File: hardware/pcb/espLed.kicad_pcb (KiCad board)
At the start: 2 copper layers, 23 parts, among them J1 led_strip, J2 flashing, J3 power, Q1 IRF9310TRPBF, Q2 AO3400A, Q3 AO3400A, Q4 AO3400A, SW1 reset, SW2 flash, U1 AMS1117-3.3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

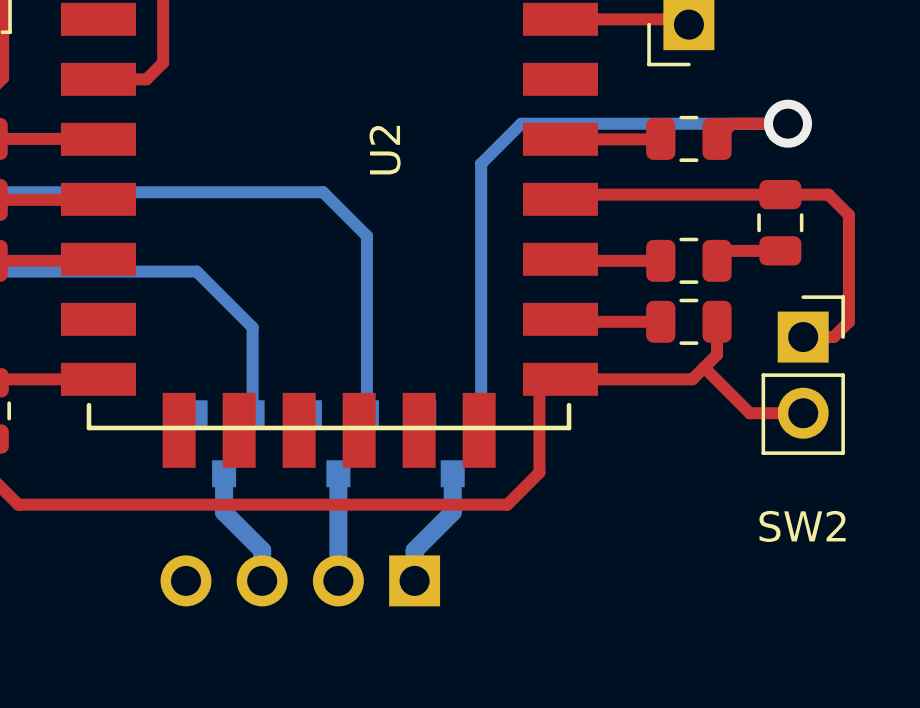
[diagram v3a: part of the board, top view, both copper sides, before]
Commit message: move the 'flash' jumper to save a bit of space
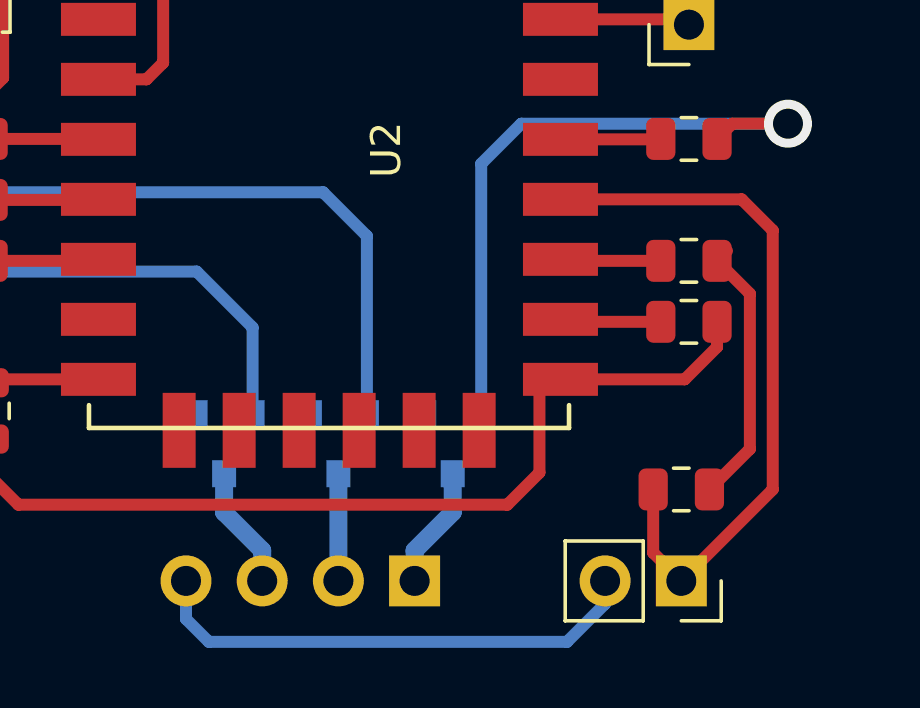
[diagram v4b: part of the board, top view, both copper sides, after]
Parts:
- moved R7 9.48 mm to (191.0, 135.9), turned to 180 degrees
- moved SW2 9.09 mm to (191.0, 138.9), turned to 270 degrees
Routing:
- net GND: track 62.3 -> 75.1 mm
- net Net-(R7-Pad2): track 16.0 -> 24.8 mm
- net +3V3: track 17.4 -> 24.3 mm
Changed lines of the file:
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@@
     (thickness 1.6)
     (drawings 0)
-    (tracks 115)
+    (tracks 119)
     (zones 0)
     (modules 23)
@@
     (pad_to_mask_clearance 0.05)
     (aux_axis_origin 0 0)
-    (visible_elements FFFFFF7F)
+    (visible_elements FFFFF77F)
     (pcbplotparams
       (layerselection 0x010fc_ffffffff)
@@
   )
   (module Connector_PinSocket_2.54mm:PinSocket_1x02_P2.54mm_Vertical (layer F.Cu)
-    (at 195.072 130.81)
+    (at 191.008 138.938 270)
     (descr "Through hole straight socket strip, 1x02, 2.54mm pitch, single row (from Kicad 4.0.7), script generated")
     (tags "Through hole socket strip THT 1x02 2.54mm single row")
-    (fp_text reference SW2 (at 0 6.35) (layer F.SilkS)
-      (effects (font (size 1 1) (thickness 0.15)))
-    )
-    (fp_text value flash (at 0 5.08) (layer F.Fab)
+    (fp_text reference SW2 (at 4.318 1.27 180) (layer F.SilkS) hide
+      (effects (font (size 1 1) (thickness 0.15)))
+    )
+    (fp_text value flash (at 0 -2.54 270) (layer F.Fab)
       (effects (font (size 1 1) (thickness 0.15)))
     )
@@
     (fp_line (start 0.635 -1.27) (end 1.27 -0.635) (layer F.Fab) (width 0.1))
     (fp_line (start -1.27 -1.27) (end 0.635 -1.27) (layer F.Fab) (width 0.1))
-    (fp_text user %R (at 0 1.27) (layer F.Fab) hide
-      (effects (font (size 1 1) (thickness 0.15)))
-    )
-    (pad 2 thru_hole oval (at 0 2.54) (size 1.7 1.7) (drill 1) (layers *.Cu *.Mask)
-      (net 1 GND))
-    (pad 1 thru_hole rect (at 0 0) (size 1.7 1.7) (drill 1) (layers *.Cu *.Mask)
+    (fp_text user %R (at 0 1.27 90) (layer F.Fab) hide
+      (effects (font (size 1 1) (thickness 0.15)))
+    )
+    (pad 2 thru_hole oval (at 0 2.54 270) (size 1.7 1.7) (drill 1) (layers *.Cu *.Mask)
+      (net 1 GND))
+    (pad 1 thru_hole rect (at 0 0 270) (size 1.7 1.7) (drill 1) (layers *.Cu *.Mask)
       (net 19 "Net-(R7-Pad2)"))
     (model ${KISYS3DMOD}/Connector_PinSocket_2.54mm.3dshapes/PinSocket_1x02_P2.54mm_Vertical.wrl
@@
   )
   (module Resistor_SMD:R_0805_2012Metric (layer F.Cu)
-    (at 194.31 127 90)
+    (at 191.008 135.89 180)
     (descr "Resistor SMD 0805 (2012 Metric), square (rectangular) end terminal, IPC_7351 nominal, (Body size source: https://docs.google.com/spreadsheets/d/1BsfQQcO9C6DZCsRaXUlFlo91Tg2WpOkGARC1WS5S8t0/edit?usp=sharing), generated with kicad-footprint-generator")
     (tags resistor)
     (attr smd)
-    (fp_text reference R7 (at 0 -1.65 90) (layer F.SilkS) hide
-      (effects (font (size 1 1) (thickness 0.15)))
-    )
-    (fp_text value 10k (at 0 1.65 90) (layer F.Fab) hide
+    (fp_text reference R7 (at 0 -1.65) (layer F.SilkS) hide
+      (effects (font (size 1 1) (thickness 0.15)))
+    )
+    (fp_text value 10k (at 0 1.65) (layer F.Fab) hide
       (effects (font (size 1 1) (thickness 0.15)))
     )
@@
     (fp_line (start -1 -0.6) (end 1 -0.6) (layer F.Fab) (width 0.1))
     (fp_line (start -1 0.6) (end -1 -0.6) (layer F.Fab) (width 0.1))
-    (fp_text user %R (at 0 0 90) (layer F.Fab) hide
+    (fp_text user %R (at 0 0) (layer F.Fab) hide
       (effects (font (size 0.5 0.5) (thickness 0.08)))
     )
-    (pad 2 smd roundrect (at 0.9375 0 90) (size 0.975 1.4) (layers F.Cu F.Paste F.Mask) (roundrect_rratio 0.25)
+    (pad 2 smd roundrect (at 0.9375 0 180) (size 0.975 1.4) (layers F.Cu F.Paste F.Mask) (roundrect_rratio 0.25)
       (net 19 "Net-(R7-Pad2)"))
-    (pad 1 smd roundrect (at -0.9375 0 90) (size 0.975 1.4) (layers F.Cu F.Paste F.Mask) (roundrect_rratio 0.25)
+    (pad 1 smd roundrect (at -0.9375 0 180) (size 0.975 1.4) (layers F.Cu F.Paste F.Mask) (roundrect_rratio 0.25)
       (net 3 +3V3))
     (model ${KISYS3DMOD}/Resistor_SMD.3dshapes/R_0805_2012Metric.wrl
@@
   (segment (start 167.894 135.382) (end 168.91 136.398) (width 0.4) (layer F.Cu) (net 1))
   (segment (start 167.894 134.209) (end 167.894 135.382) (width 0.4) (layer F.Cu) (net 1))
-  (segment (start 191.376 132.22) (end 186.28 132.22) (width 0.4) (layer F.Cu) (net 1))
-  (segment (start 192.1995 130.302) (end 192.1995 131.3965) (width 0.4) (layer F.Cu) (net 1))
-  (segment (start 193.294 133.35) (end 191.77 131.826) (width 0.4) (layer F.Cu) (net 1))
-  (segment (start 195.072 133.35) (end 193.294 133.35) (width 0.4) (layer F.Cu) (net 1))
-  (segment (start 191.77 131.826) (end 191.376 132.22) (width 0.4) (layer F.Cu) (net 1))
-  (segment (start 192.1995 131.3965) (end 191.77 131.826) (width 0.4) (layer F.Cu) (net 1))
+  (segment (start 192.1995 131.1425) (end 192.1995 130.302) (width 0.4) (layer F.Cu) (net 1))
+  (segment (start 191.122 132.22) (end 192.1995 131.1425) (width 0.4) (layer F.Cu) (net 1))
+  (segment (start 186.28 132.22) (end 191.122 132.22) (width 0.4) (layer F.Cu) (net 1))
+  (segment (start 174.498 140.208) (end 174.498 138.938) (width 0.4) (layer B.Cu) (net 1))
+  (segment (start 175.26 140.97) (end 174.498 140.208) (width 0.4) (layer B.Cu) (net 1))
+  (segment (start 187.198 140.97) (end 175.26 140.97) (width 0.4) (layer B.Cu) (net 1))
+  (segment (start 188.468 139.7) (end 187.198 140.97) (width 0.4) (layer B.Cu) (net 1))
+  (segment (start 188.468 138.938) (end 188.468 139.7) (width 0.4) (layer B.Cu) (net 1))
   (segment (start 47.75 71.95) (end 47.8 71.9) (width 0.4) (layer F.Cu) (net 2))
   (segment (start 47.75 74.3125) (end 47.75 71.95) (width 0.4) (layer F.Cu) (net 2))
@@
   (segment (start 172.28 132.22) (end 168.008 132.22) (width 0.4) (layer F.Cu) (net 3))
   (segment (start 192.532 127.9375) (end 192.1995 128.27) (width 0.4) (layer F.Cu) (net 3))
-  (segment (start 194.31 127.9375) (end 192.532 127.9375) (width 0.4) (layer F.Cu) (net 3))
   (segment (start 166.1945 110.49) (end 166.1945 112.522) (width 0.4) (layer F.Cu) (net 3))
+  (segment (start 193.294 134.5415) (end 191.9455 135.89) (width 0.4) (layer F.Cu) (net 3))
+  (segment (start 193.294 129.3645) (end 193.294 134.5415) (width 0.4) (layer F.Cu) (net 3))
+  (segment (start 192.1995 128.27) (end 193.294 129.3645) (width 0.4) (layer F.Cu) (net 3))
   (segment (start 175.768 136.652) (end 177.038 137.922) (width 0.6) (layer B.Cu) (net 4))
   (segment (start 177.038 137.922) (end 177.038 138.938) (width 0.6) (layer B.Cu) (net 4))
@@
   (segment (start 172.28 122.22) (end 173.182 122.22) (width 0.4) (layer F.Cu) (net 18))
   (segment (start 186.28 126.22) (end 186.298 126.238) (width 0.4) (layer F.Cu) (net 19))
-  (segment (start 196.088 130.81) (end 195.072 130.81) (width 0.4) (layer F.Cu) (net 19))
-  (segment (start 196.596 130.302) (end 196.088 130.81) (width 0.4) (layer F.Cu) (net 19))
-  (segment (start 195.9125 126.0625) (end 196.596 126.746) (width 0.4) (layer F.Cu) (net 19))
-  (segment (start 196.596 126.746) (end 196.596 130.302) (width 0.4) (layer F.Cu) (net 19))
-  (segment (start 194.31 126.0625) (end 195.9125 126.0625) (width 0.4) (layer F.Cu) (net 19))
   (segment (start 186.4375 126.0625) (end 186.28 126.22) (width 0.4) (layer F.Cu) (net 19))
-  (segment (start 194.31 126.0625) (end 186.4375 126.0625) (width 0.4) (layer F.Cu) (net 19))
+  (segment (start 190.0705 138.0005) (end 191.008 138.938) (width 0.4) (layer F.Cu) (net 19))
+  (segment (start 190.0705 135.89) (end 190.0705 138.0005) (width 0.4) (layer F.Cu) (net 19))
+  (segment (start 194.056 127.254) (end 194.056 135.89) (width 0.4) (layer F.Cu) (net 19))
+  (segment (start 193.022 126.22) (end 194.056 127.254) (width 0.4) (layer F.Cu) (net 19))
+  (segment (start 194.056 135.89) (end 191.008 138.938) (width 0.4) (layer F.Cu) (net 19))
+  (segment (start 186.28 126.22) (end 193.022 126.22) (width 0.4) (layer F.Cu) (net 19))
   (segment (start 186.33 128.27) (end 186.28 128.22) (width 0.4) (layer F.Cu) (net 20))
   (segment (start 190.3245 128.27) (end 186.33 128.27) (width 0.4) (layer F.Cu) (net 20))

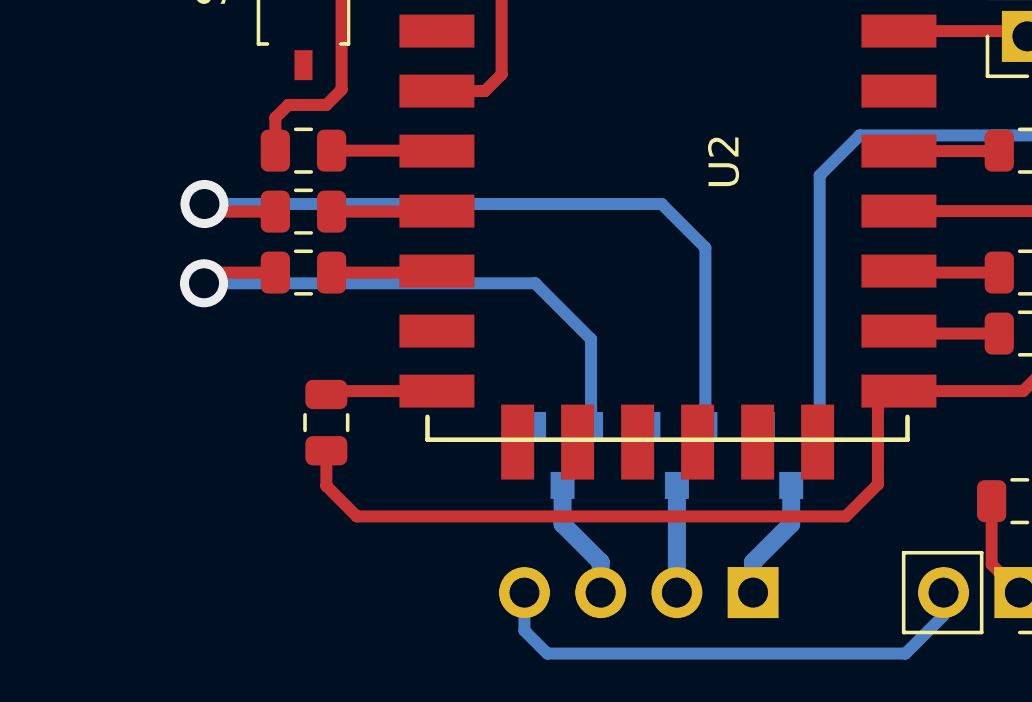
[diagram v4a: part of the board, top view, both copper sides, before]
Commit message: rearrange vias on the left side to save a bit of space
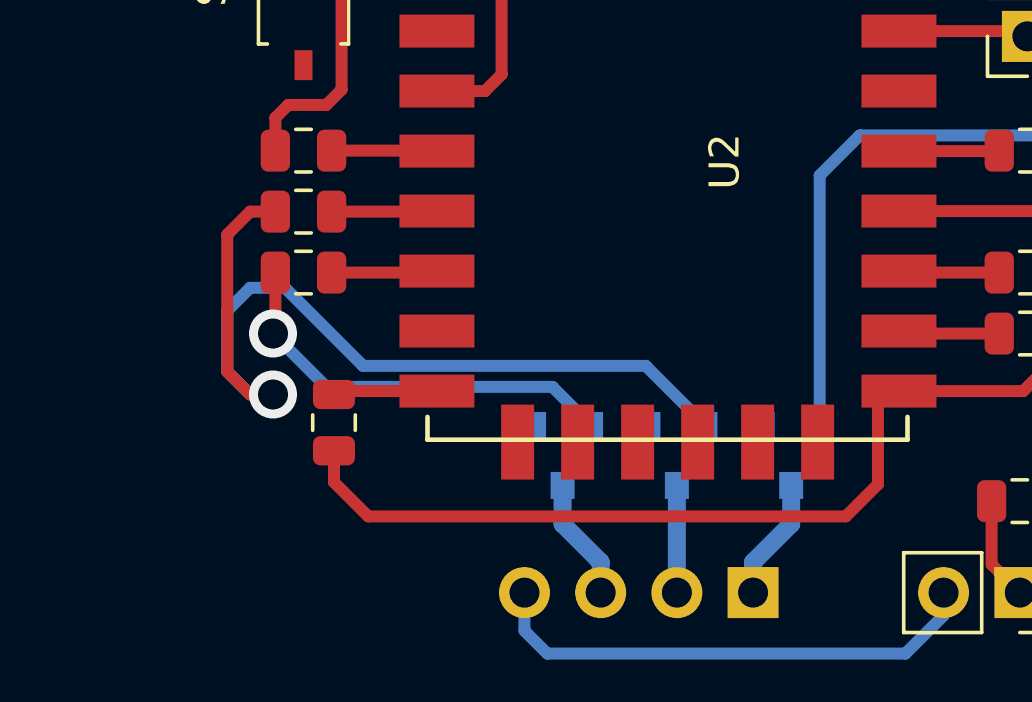
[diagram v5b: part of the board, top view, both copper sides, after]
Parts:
- moved C3 0.25 mm to (168.1, 133.3)
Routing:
- net Net-(Q4-Pad2): track 19.1 -> 13.9 mm
- net Net-(Q3-Pad2): track 25.7 -> 30.4 mm

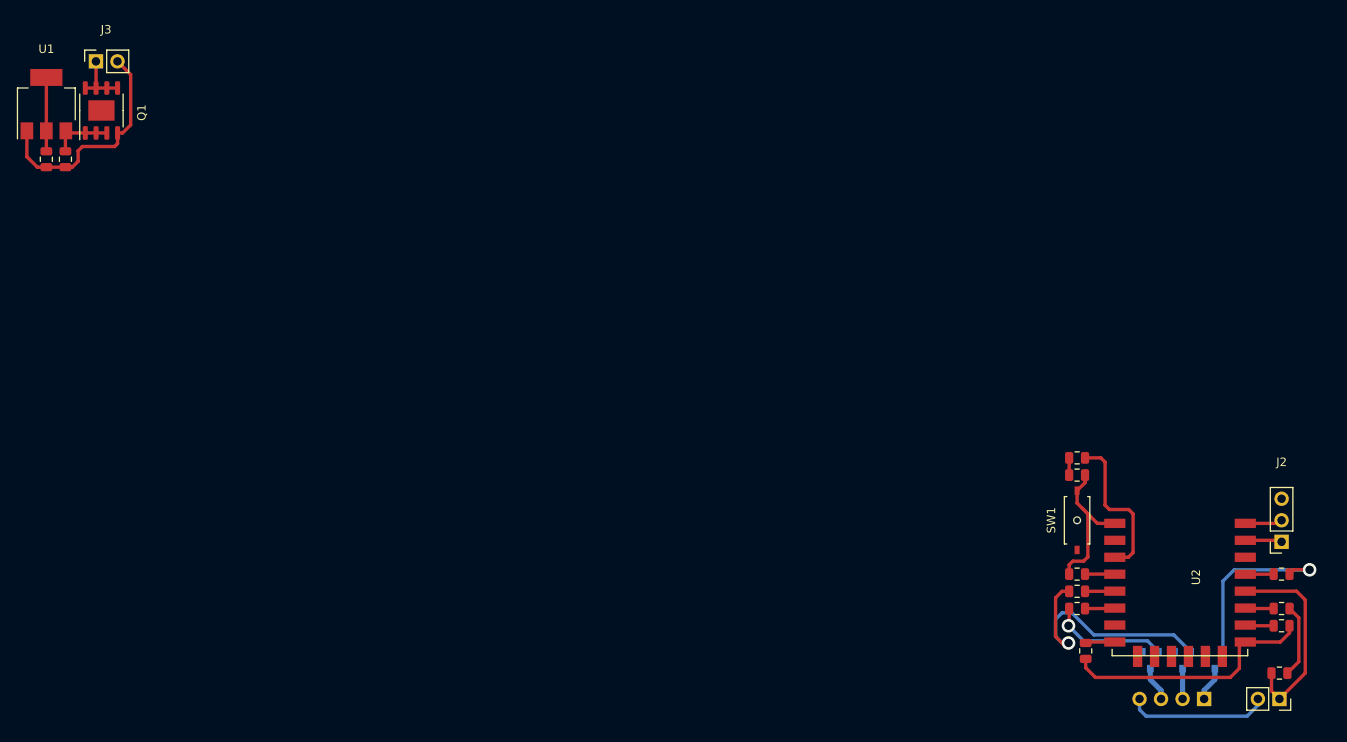
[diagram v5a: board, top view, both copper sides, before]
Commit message: arrange components on the right side tighter
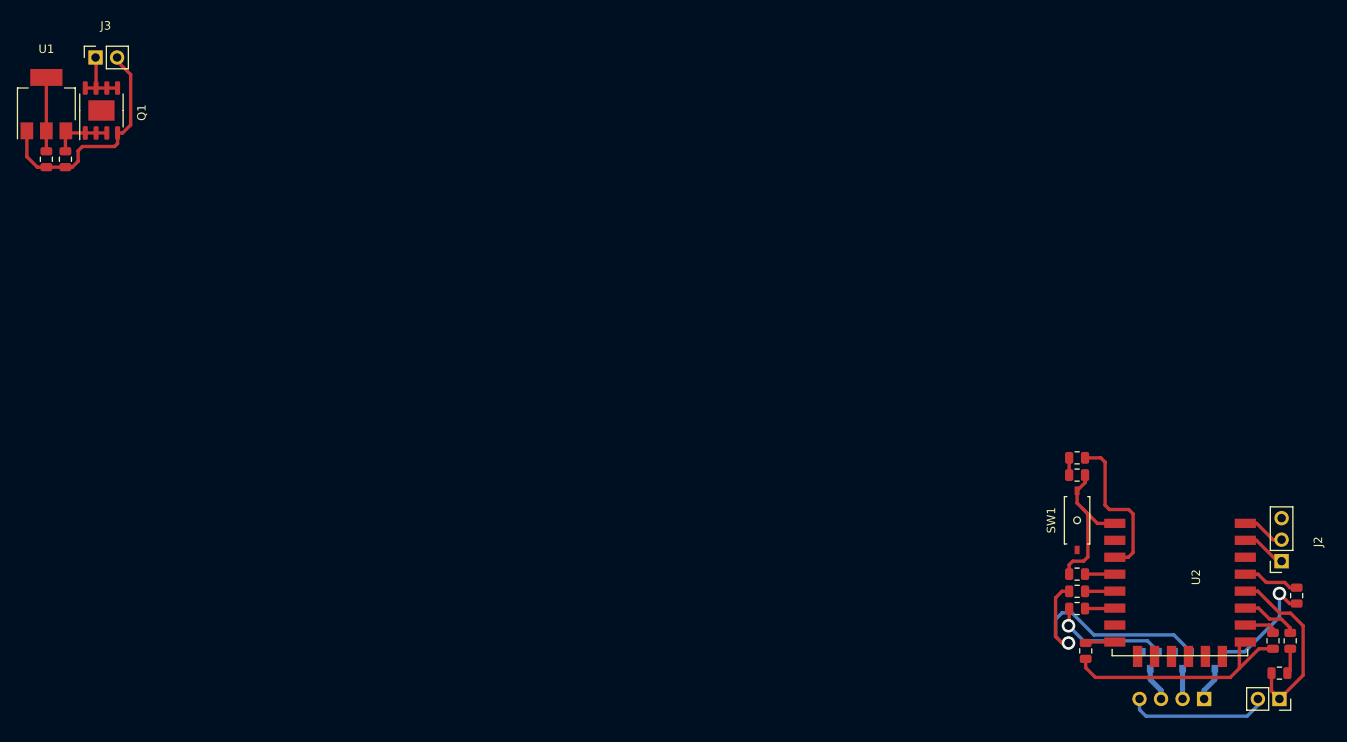
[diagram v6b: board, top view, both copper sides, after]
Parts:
- moved R8 3.94 mm to (192.3, 132.1), turned to 90 degrees
- moved R3 3.10 mm to (193.0, 126.7), turned to 90 degrees
- moved J2 2.29 mm to (191.3, 122.7)
- moved R9 2.05 mm to (190.2, 132.1), turned to 90 degrees
- moved J3 0.46 mm to (51.3, 63.2)
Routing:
- net Net-(Q2-Pad2): track 21.7 -> 13.7 mm
- net +3V3: track 24.3 -> 18.2 mm
- net Net-(R8-Pad2): track 4.07 -> 7.62 mm
- net /led1: track 4.07 -> 7.55 mm
- net GND: track 74.7 -> 72.5 mm
- net Net-(R7-Pad2): track 24.8 -> 22.7 mm
- net /TX: track 5.05 -> 6.00 mm
- net Net-(R9-Pad2): track 4.08 -> 4.75 mm
- net /RX: track 5.13 -> 5.78 mm

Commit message: place power part into it's position and connect some of the power pins
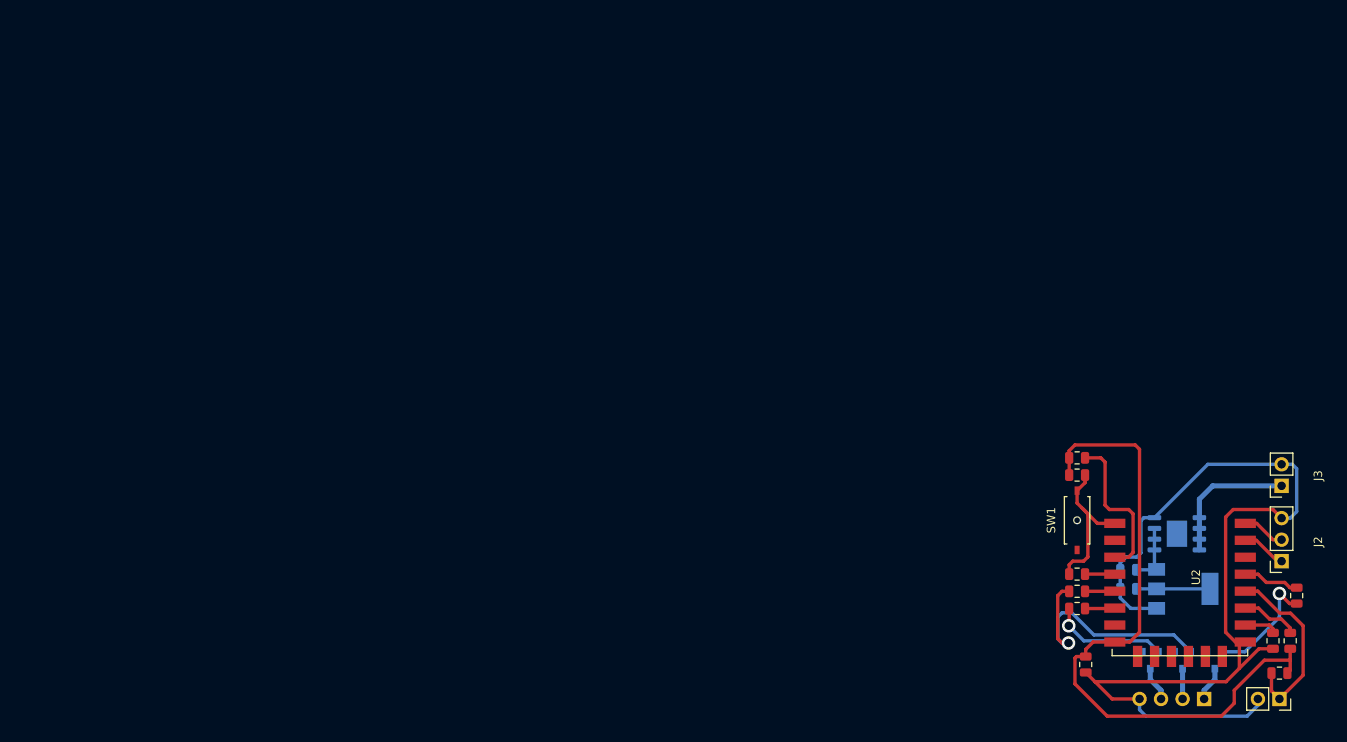
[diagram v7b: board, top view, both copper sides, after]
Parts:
- C1, C2, Q1, U1: moved to B.Cu
- moved J3 148.8 mm to (191.3, 113.8), turned to 180 degrees
- moved U1 145.8 mm to (179.7, 126.0), turned to 0 degrees
- moved C2 137.4 mm to (173.2, 126.0), turned to 180 degrees
- moved Q1 136.4 mm to (178.9, 119.5), turned to 0 degrees
- moved C1 134.4 mm to (173.2, 123.7), turned to 180 degrees
- moved C3 1.60 mm to (168.1, 134.9)
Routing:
- net +3V3: track 18.2 -> 88.6 mm
- net GND: track 72.5 -> 117.5 mm
- net /12v_in: track 6.97 -> 16.3 mm
